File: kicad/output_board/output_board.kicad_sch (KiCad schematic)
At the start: 22 parts, among them J1 DRV1, J2 DRV2, J3 CH_OUT, U1 TPS5430DDA, U2 LM324DT

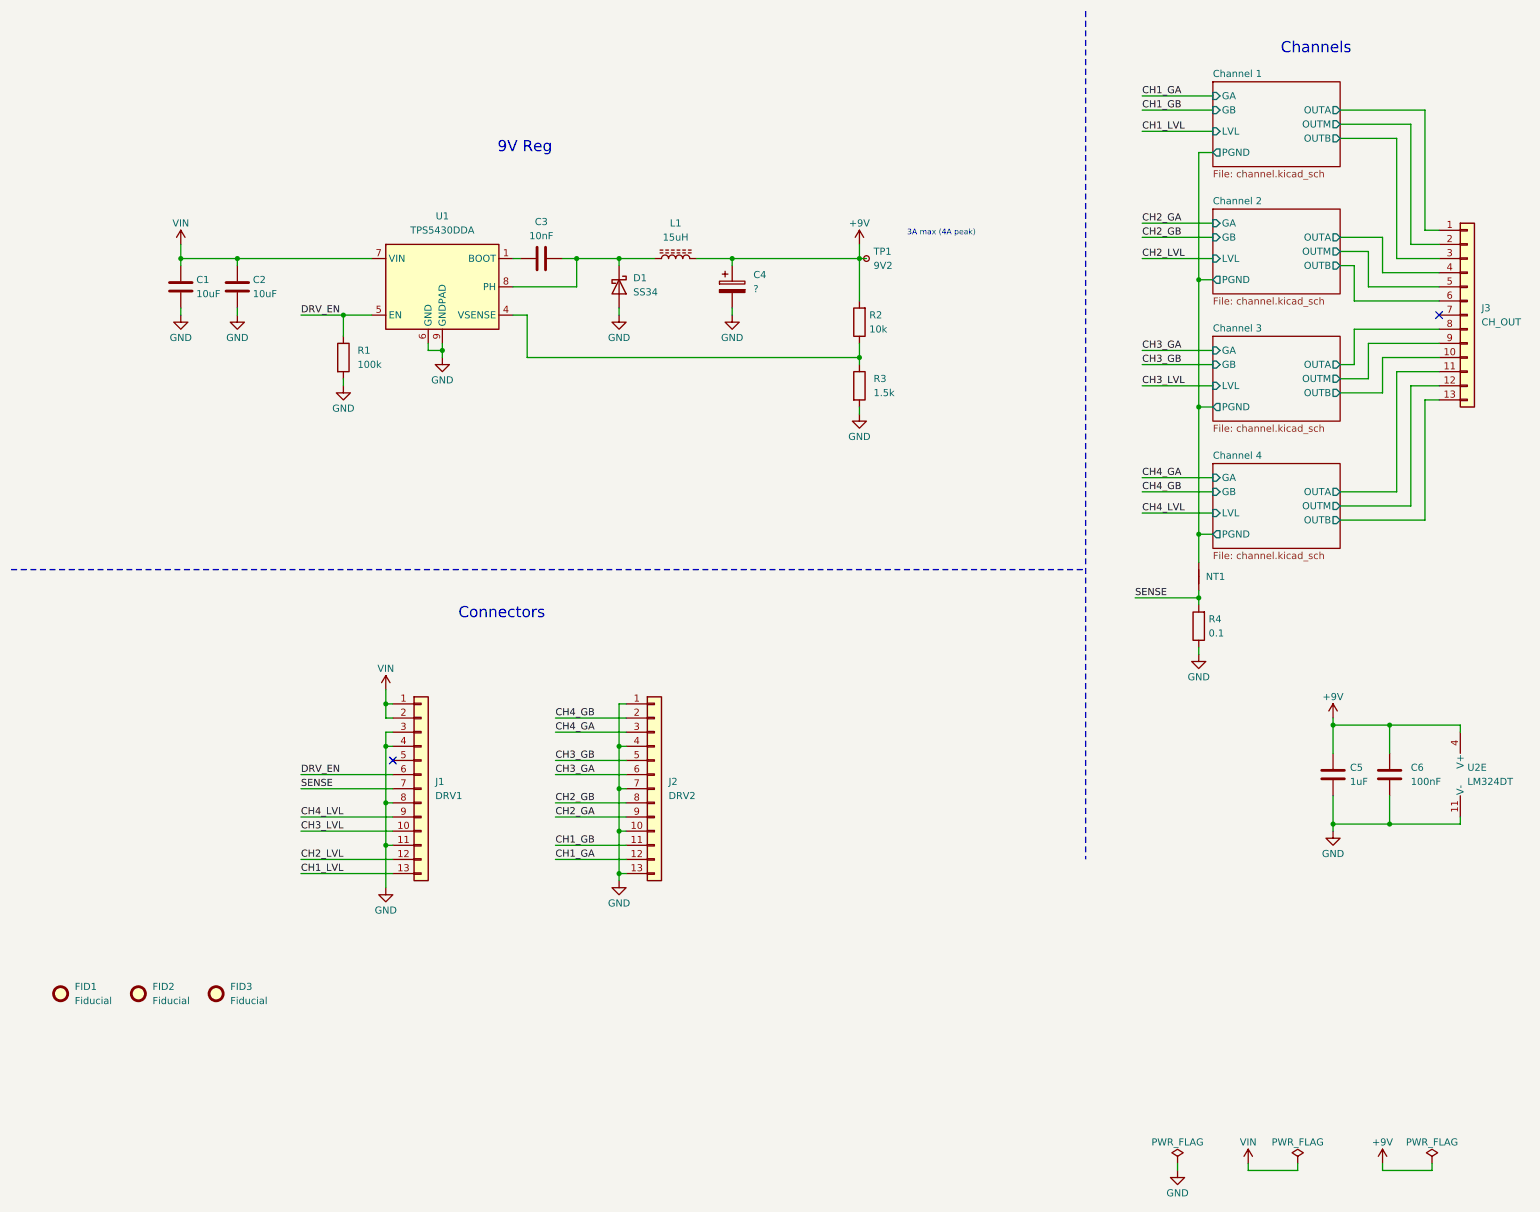
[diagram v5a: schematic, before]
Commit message: add capacitors
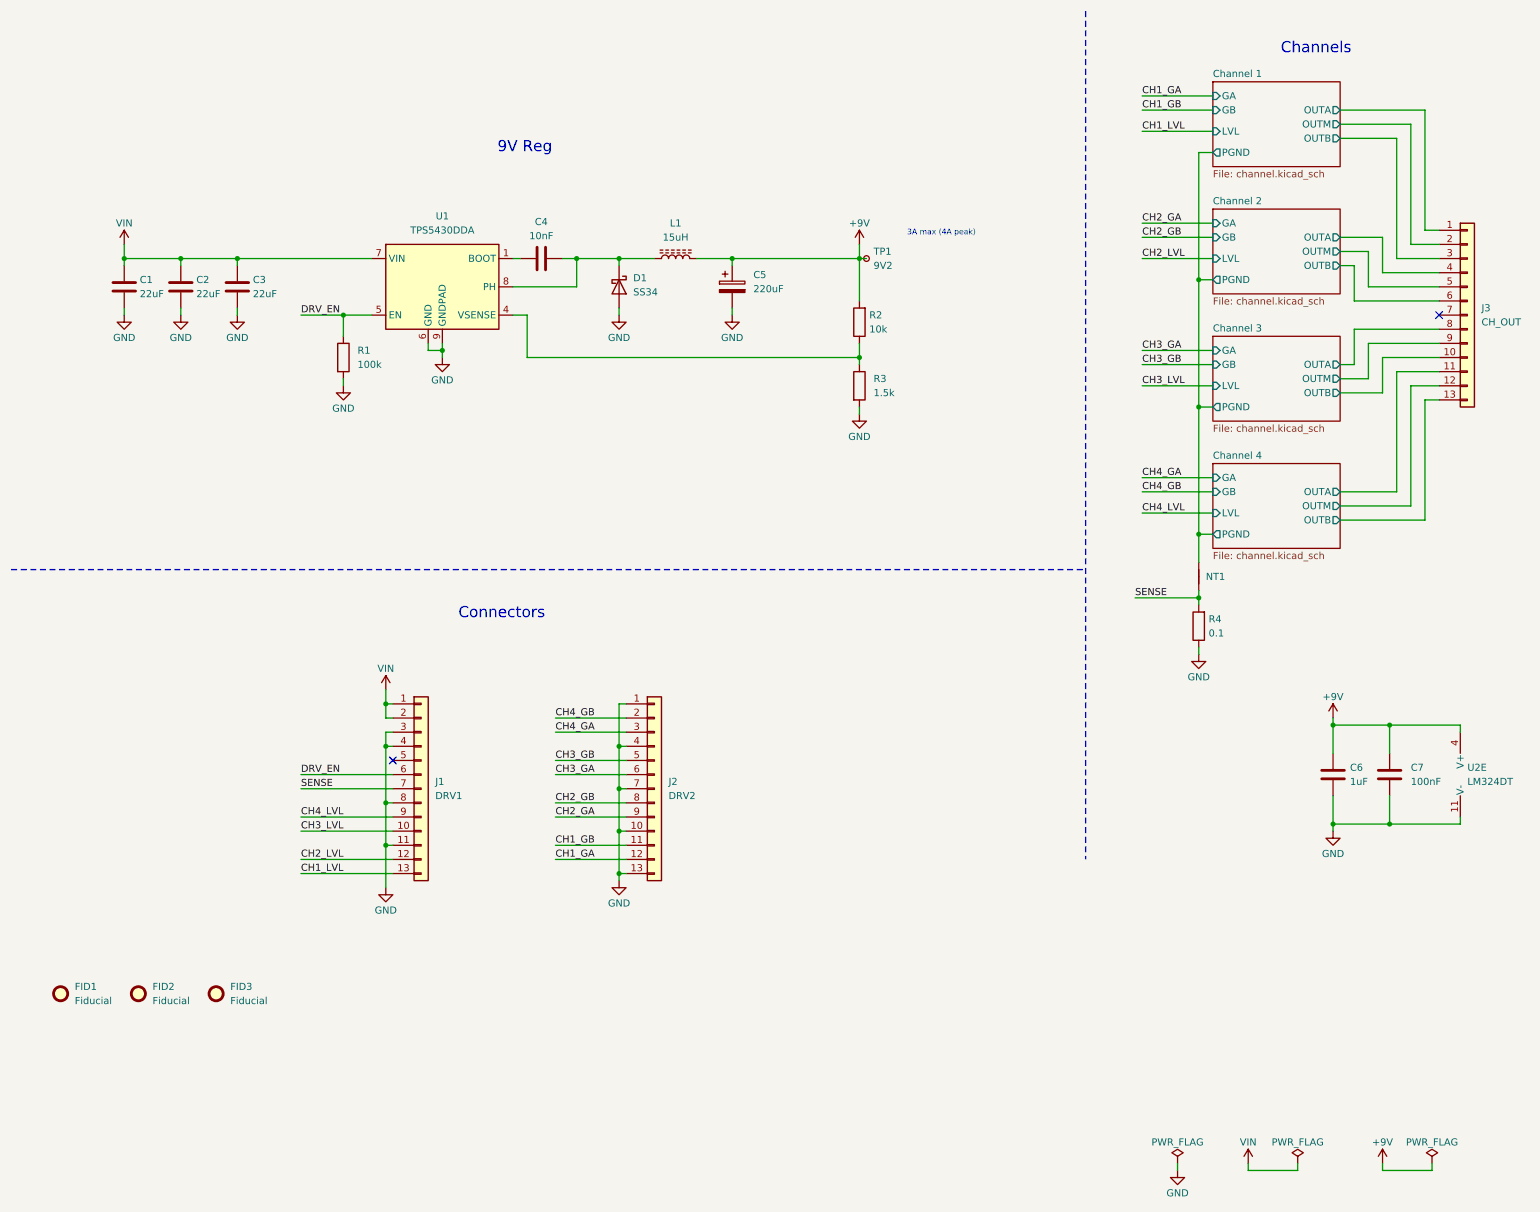
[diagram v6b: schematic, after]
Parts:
- removed C2: 10uF, Capacitor_SMD:C_0805_2012Metric, symbol Device:C
- added C1, C3: 22uF, Capacitor_SMD:C_0805_2012Metric, symbol Device:C
- C2: renamed from C1; value 10uF -> 22uF; LCSC C440198 -> C45783
- C5: renamed from C4; value ? -> 220uF; footprint (none) -> Capacitor_THT:CP_Radial_D8.0mm_P3.50mm; LCSC (none) -> C264063; Service (none) -> HandAssembly
- renumbered C3 to C4, C5 to C6, C6 to C7
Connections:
- net GND: now also C1.1, C3.1
- net VIN: now also C1.2, C3.2

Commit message: add inductor footprint
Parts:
- L1: footprint ~ -> SaawLib:L_CJIANG_FXL0630
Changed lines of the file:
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@@
 			)
 		)
-		(property "Footprint" "~"
+		(property "Footprint" "SaawLib:L_CJIANG_FXL0630"
 			(at 132.08 57.15 0)
 			(effects

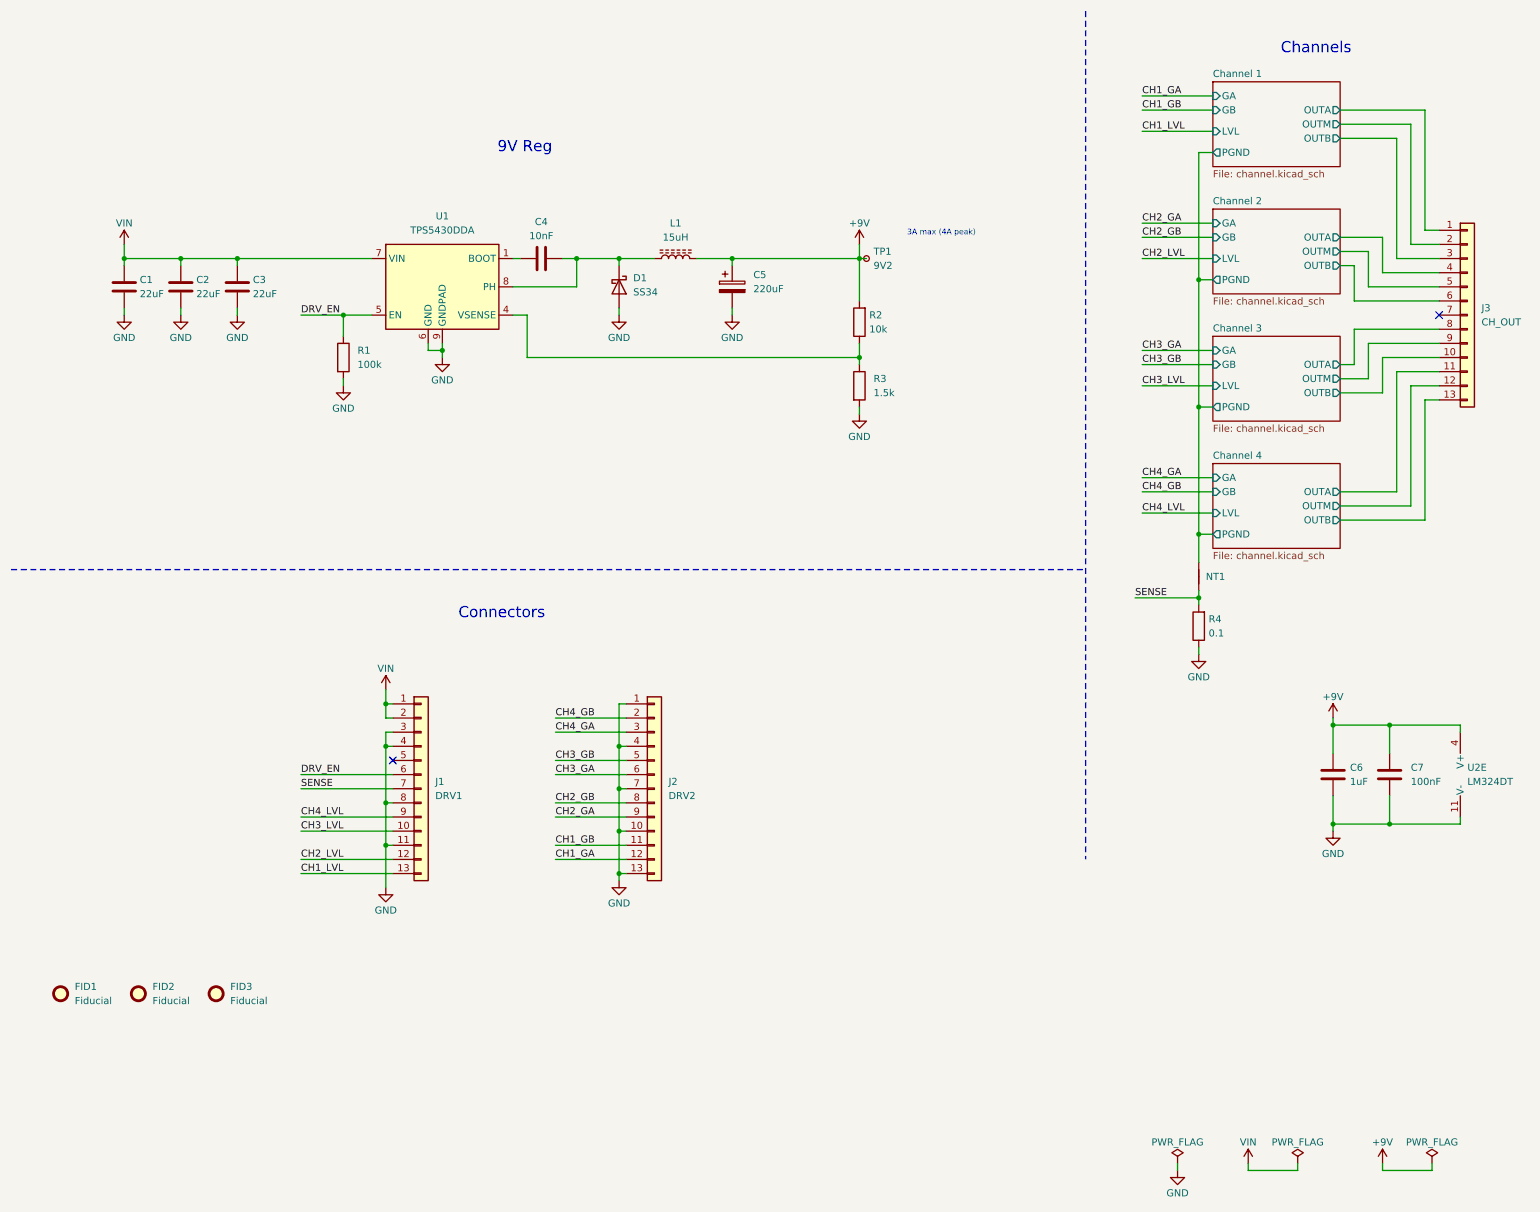
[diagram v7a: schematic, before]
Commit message: use 2x8 pin header
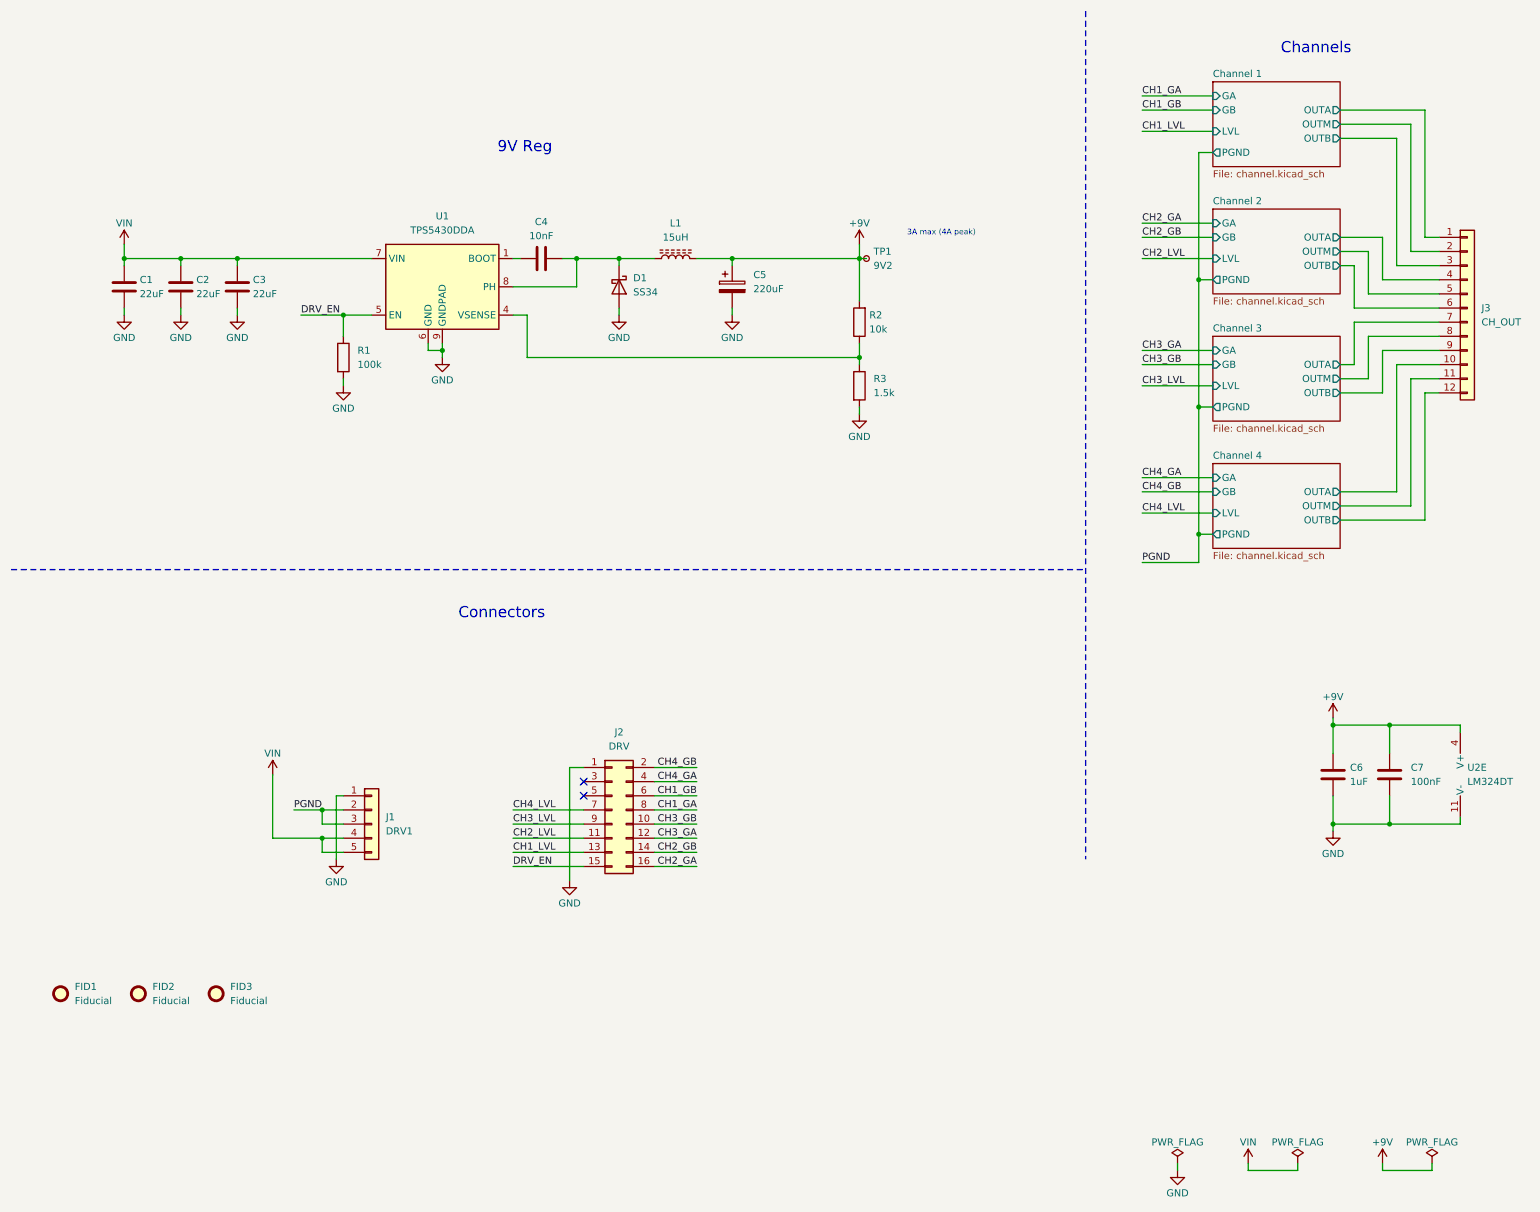
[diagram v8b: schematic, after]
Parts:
- removed J2: DRV2, Connector_PinSocket_2.54mm:PinSocket_1x13_P2.54mm_Vertical, symbol Connector_Generic:Conn_01x13
- removed NT1: ~, NetTie:NetTie-2_SMD_Pad2.0mm, symbol Device:NetTie_2
- removed R4: 0.1, Resistor_SMD:R_2512_6332Metric, symbol Device:R
- added J2: DRV, Connector_PinHeader_2.54mm:PinHeader_2x08_P2.54mm_Vertical, symbol Connector_Generic:Conn_02x08_Odd_Even
- J1: footprint Connector_PinSocket_2.54mm:PinSocket_1x13_P2.54mm_Vertical -> Connector_PinHeader_2.54mm:PinHeader_1x05_P2.54mm_Vertical; symbol Connector_Generic:Conn_01x13 -> Connector_Generic:Conn_01x05; LCSC C2897376 -> C492404
- J3: footprint Connector_PinSocket_2.54mm:PinSocket_1x13_P2.54mm_Vertical -> Connector_PinSocket_2.54mm:PinSocket_1x12_P2.54mm_Vertical; symbol Connector_Generic:Conn_01x13 -> Connector_Generic:Conn_01x12; LCSC C2897376 -> C2897375
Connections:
- net CH1_GA: now also J2.8 (Pin_8)
- net CH1_GB: now also J2.6 (Pin_6)
- net CH1_LVL: now also J2.13 (Pin_13); no longer J1.13 (Pin_13)
- net CH2_GA: now also J2.16 (Pin_16)
- net CH2_GB: now also J2.14 (Pin_14)
- net CH2_LVL: now also J2.11 (Pin_11); no longer J1.12 (Pin_12)
- net CH3_GA: now also J2.12 (Pin_12)
- net CH3_GB: now also J2.10 (Pin_10)
- net CH3_LVL: now also J2.9 (Pin_9); no longer J1.10 (Pin_10)
- net CH4_GA: now also J2.4 (Pin_4)
- net CH4_GB: now also J2.2 (Pin_2)
- net CH4_LVL: now also J2.7 (Pin_7); no longer J1.9 (Pin_9)
- net Channel 3/OUTA: now also J3.7 (Pin_7); no longer J3.8 (Pin_8)
- net Channel 3/OUTB: now also J3.9 (Pin_9); no longer J3.10 (Pin_10)
- net Channel 3/OUTM: now also J3.8 (Pin_8); no longer J3.9 (Pin_9)
- net Channel 4/OUTA: now also J3.10 (Pin_10); no longer J3.11 (Pin_11)
- net Channel 4/OUTB: now also J3.12 (Pin_12); no longer J3.13 (Pin_13)
- net Channel 4/OUTM: now also J3.11 (Pin_11); no longer J3.12 (Pin_12)
- net DRV_EN: now also J2.15 (Pin_15); no longer J1.6 (Pin_6)
- net GND: now also J1.1 (Pin_1), J2.1 (Pin_1); no longer J1.11 (Pin_11), J1.3 (Pin_3), J1.4 (Pin_4), J1.8 (Pin_8)
- net VIN: now also J1.4 (Pin_4), J1.5 (Pin_5); no longer J1.1 (Pin_1), J1.2 (Pin_2)
- removed net SENSE: J1.7 (Pin_7)
- new net PGND: J1.2 (Pin_2), J1.3 (Pin_3)
